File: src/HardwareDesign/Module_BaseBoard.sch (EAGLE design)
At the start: 84 parts, among them IC1 RT9742GGJ, IC2 AP22653W6, IC3 74LVC1G07, IC4 RT9742NGV, IC5 AP3441SHE-7B, J1 692121030100, J2 692121030100, J3 FH12-22S-0.5SVA, J4 FH12-22S-0.5SVA, SW1 1825027-8, X1 CON-VG_MAB642, X2 CRYSTAL, X3 CON-VG_MAB642

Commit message: finish PCB desing
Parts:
- C1, C10, C11, C12, C13, C2, C20, C3, C4, C5, C9: device ds_passive:C0402 -> ds_passive:C-0402
- C14, C15, C16, C17, C18, C19, C6, C7: device ds_passive:C0805 -> ds_passive:C-0805
- renumbered X1 to MODULE_AIO, X3 to MODULE_DIO

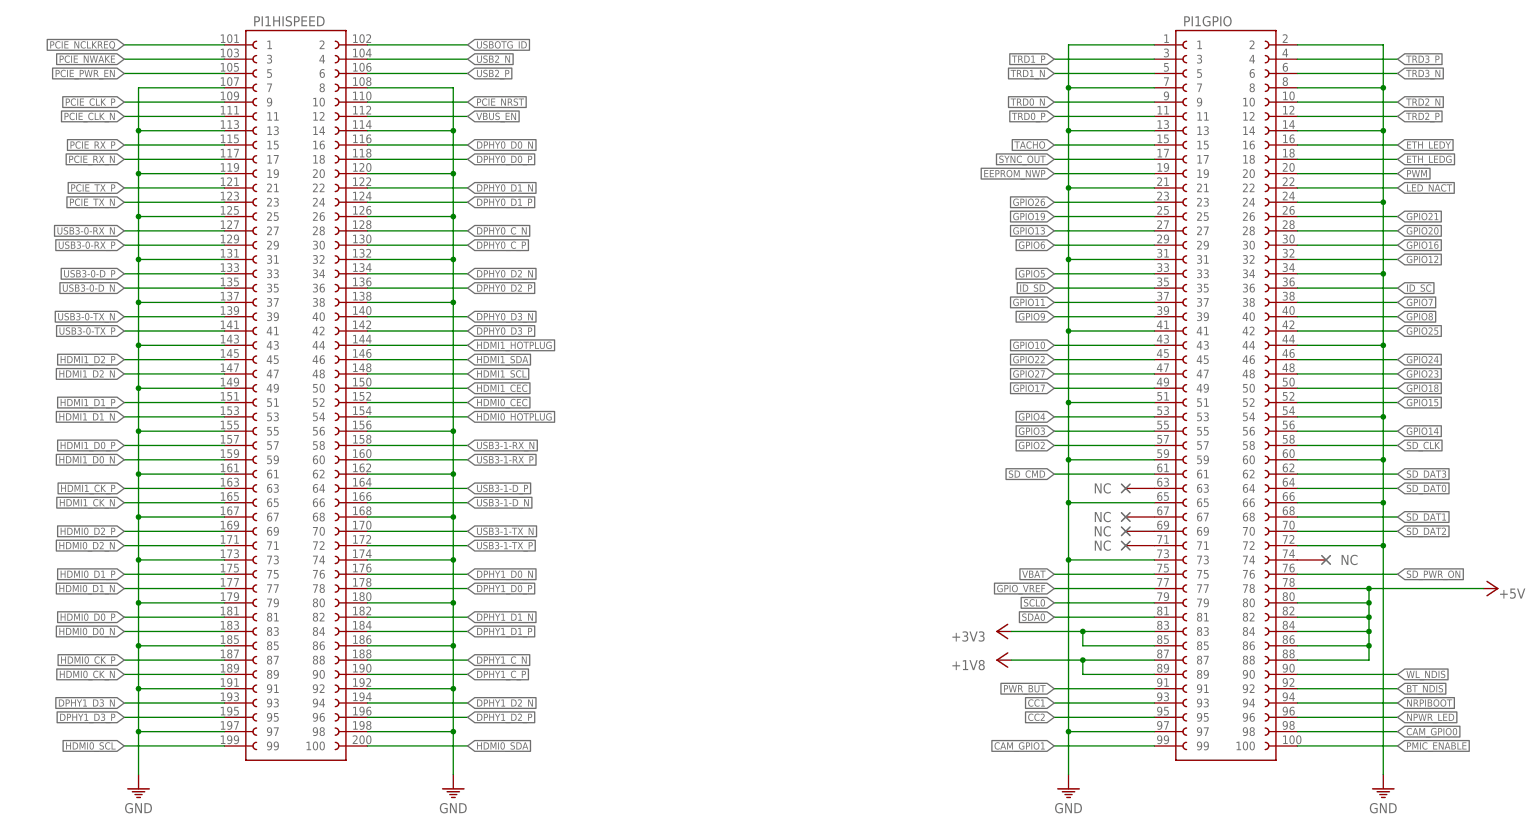
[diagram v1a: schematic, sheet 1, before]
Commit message: add diffpaircheck
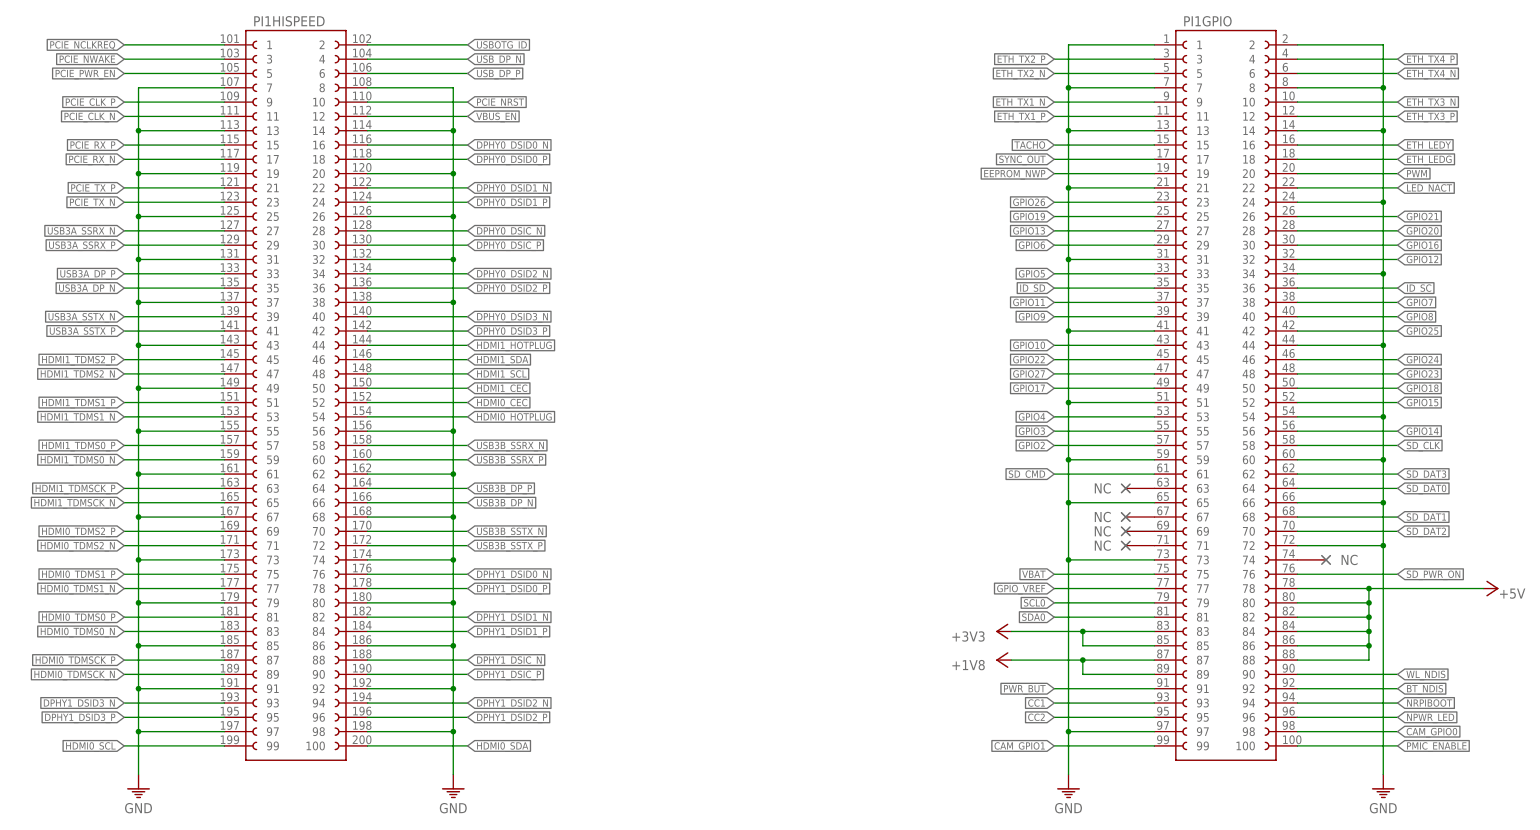
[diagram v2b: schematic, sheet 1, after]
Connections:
- net DPHY0_C_N renamed DPHY0_DSIC_N
- net DPHY0_C_P renamed DPHY0_DSIC_P
- net DPHY0_D0_N renamed DPHY0_DSID0_N
- net DPHY0_D0_P renamed DPHY0_DSID0_P
- net DPHY0_D1_N renamed DPHY0_DSID1_N
- net DPHY0_D1_P renamed DPHY0_DSID1_P
- net DPHY0_D2_N renamed DPHY0_DSID2_N
- net DPHY0_D2_P renamed DPHY0_DSID2_P
- net DPHY0_D3_N renamed DPHY0_DSID3_N
- net DPHY0_D3_P renamed DPHY0_DSID3_P
- net DPHY1_C_N renamed DPHY1_DSIC_N
- net DPHY1_C_P renamed DPHY1_DSIC_P
- net DPHY1_D0_N renamed DPHY1_DSID0_N
- net DPHY1_D0_P renamed DPHY1_DSID0_P
- net DPHY1_D1_N renamed DPHY1_DSID1_N
- net DPHY1_D1_P renamed DPHY1_DSID1_P
- net DPHY1_D2_N renamed DPHY1_DSID2_N
- net DPHY1_D2_P renamed DPHY1_DSID2_P
- net DPHY1_D3_N renamed DPHY1_DSID3_N
- net DPHY1_D3_P renamed DPHY1_DSID3_P
- net HDMI0_CK_N renamed HDMI0_TDMSCK_N
- net HDMI0_CK_P renamed HDMI0_TDMSCK_P
- net HDMI0_D0_N renamed HDMI0_TDMS0_N
- net HDMI0_D0_P renamed HDMI0_TDMS0_P
- net HDMI0_D1_N renamed HDMI0_TDMS1_N
- net HDMI0_D1_P renamed HDMI0_TDMS1_P
- net HDMI0_D2_N renamed HDMI0_TDMS2_N
- net HDMI0_D2_P renamed HDMI0_TDMS2_P
- net HDMI1_CK_N renamed HDMI1_TDMSCK_N
- net HDMI1_CK_P renamed HDMI1_TDMSCK_P
- net HDMI1_D0_N renamed HDMI1_TDMS0_N
- net HDMI1_D0_P renamed HDMI1_TDMS0_P
- net HDMI1_D1_N renamed HDMI1_TDMS1_N
- net HDMI1_D1_P renamed HDMI1_TDMS1_P
- net HDMI1_D2_N renamed HDMI1_TDMS2_N
- net HDMI1_D2_P renamed HDMI1_TDMS2_P
- net TRD0_N renamed ETH_TX1_N
- net TRD0_P renamed ETH_TX1_P
- net TRD1_N renamed ETH_TX2_N
- net TRD1_P renamed ETH_TX2_P
- net TRD2_N renamed ETH_TX3_N
- net TRD2_P renamed ETH_TX3_P
- net TRD3_N renamed ETH_TX4_N
- net TRD3_P renamed ETH_TX4_P
- net USB2_N renamed USB_DP_N
- net USB2_P renamed USB_DP_P
- net USB3-0-D_N renamed USB3A_DP_N
- net USB3-0-D_P renamed USB3A_DP_P
- net USB3-0-RX_N renamed USB3A_SSRX_N
- net USB3-0-RX_P renamed USB3A_SSRX_P
- net USB3-0-TX_N renamed USB3A_SSTX_N
- net USB3-0-TX_P renamed USB3A_SSTX_P
- net USB3-1-D_N renamed USB3B_DP_N
- net USB3-1-D_P renamed USB3B_DP_P
- net USB3-1-RX_N renamed USB3B_SSRX_N
- net USB3-1-RX_P renamed USB3B_SSRX_P
- net USB3-1-TX_N renamed USB3B_SSTX_N
- net USB3-1-TX_P renamed USB3B_SSTX_P
